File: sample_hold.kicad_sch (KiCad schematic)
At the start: 44 parts, among them K21 G6K-2FY, 5V, Q201 AO3400A, Q202 AO3401A, Q203 AO3400A, Q204 AO3400A, Q205 AO3400A, Q206 AO3400A, Q207 AO3400A, U19 TCA0372, U21 OPA828DGN, U22 OPA2197D, U23 DG419D

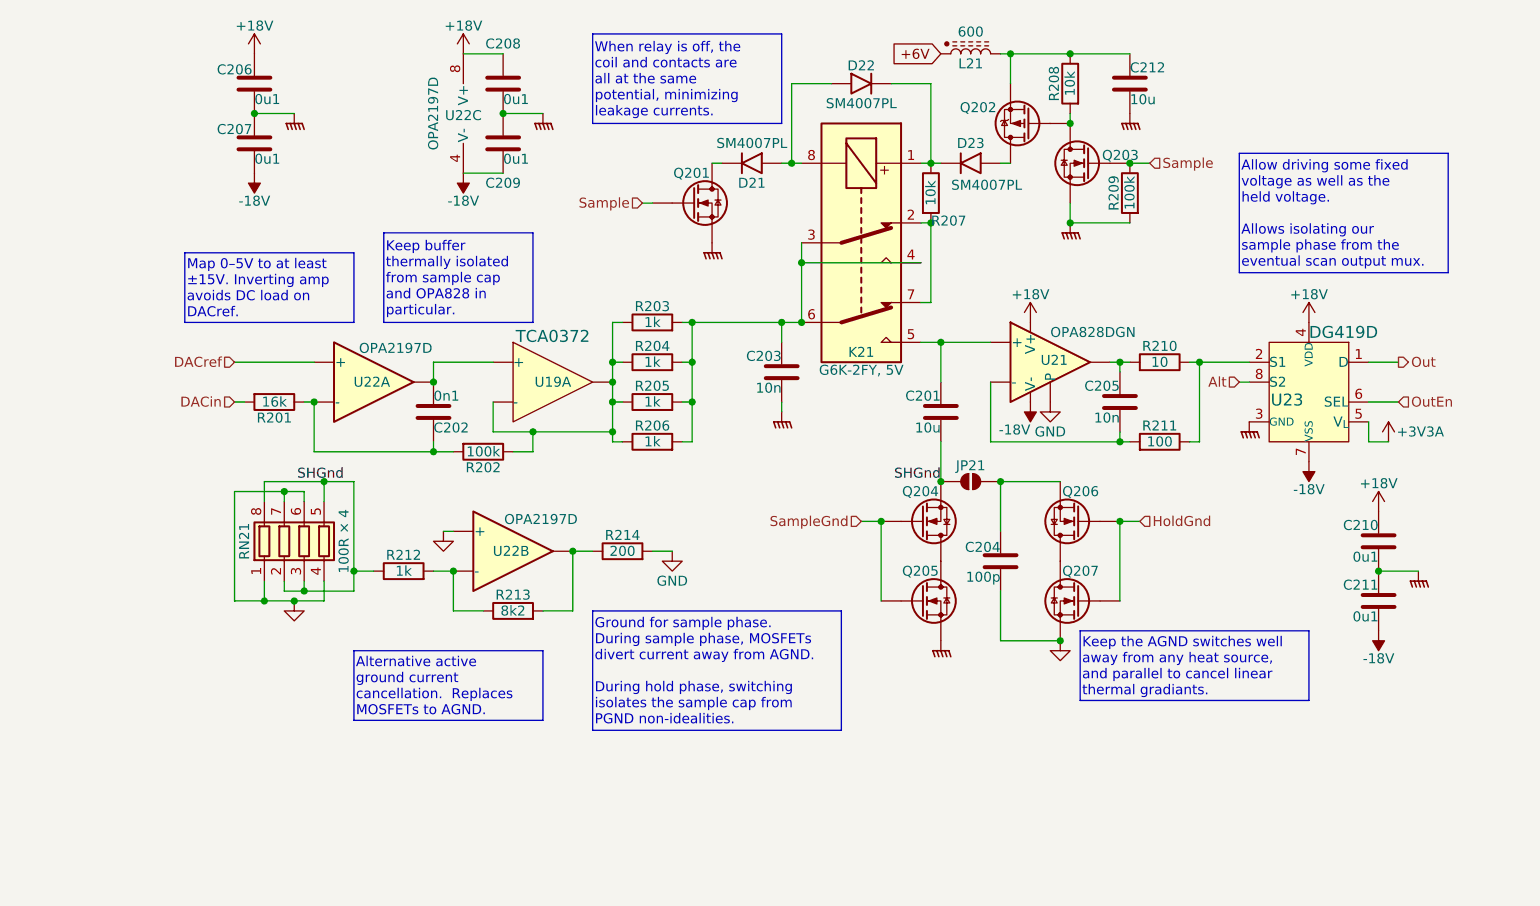
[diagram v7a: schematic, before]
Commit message: Whew.  DACs routed
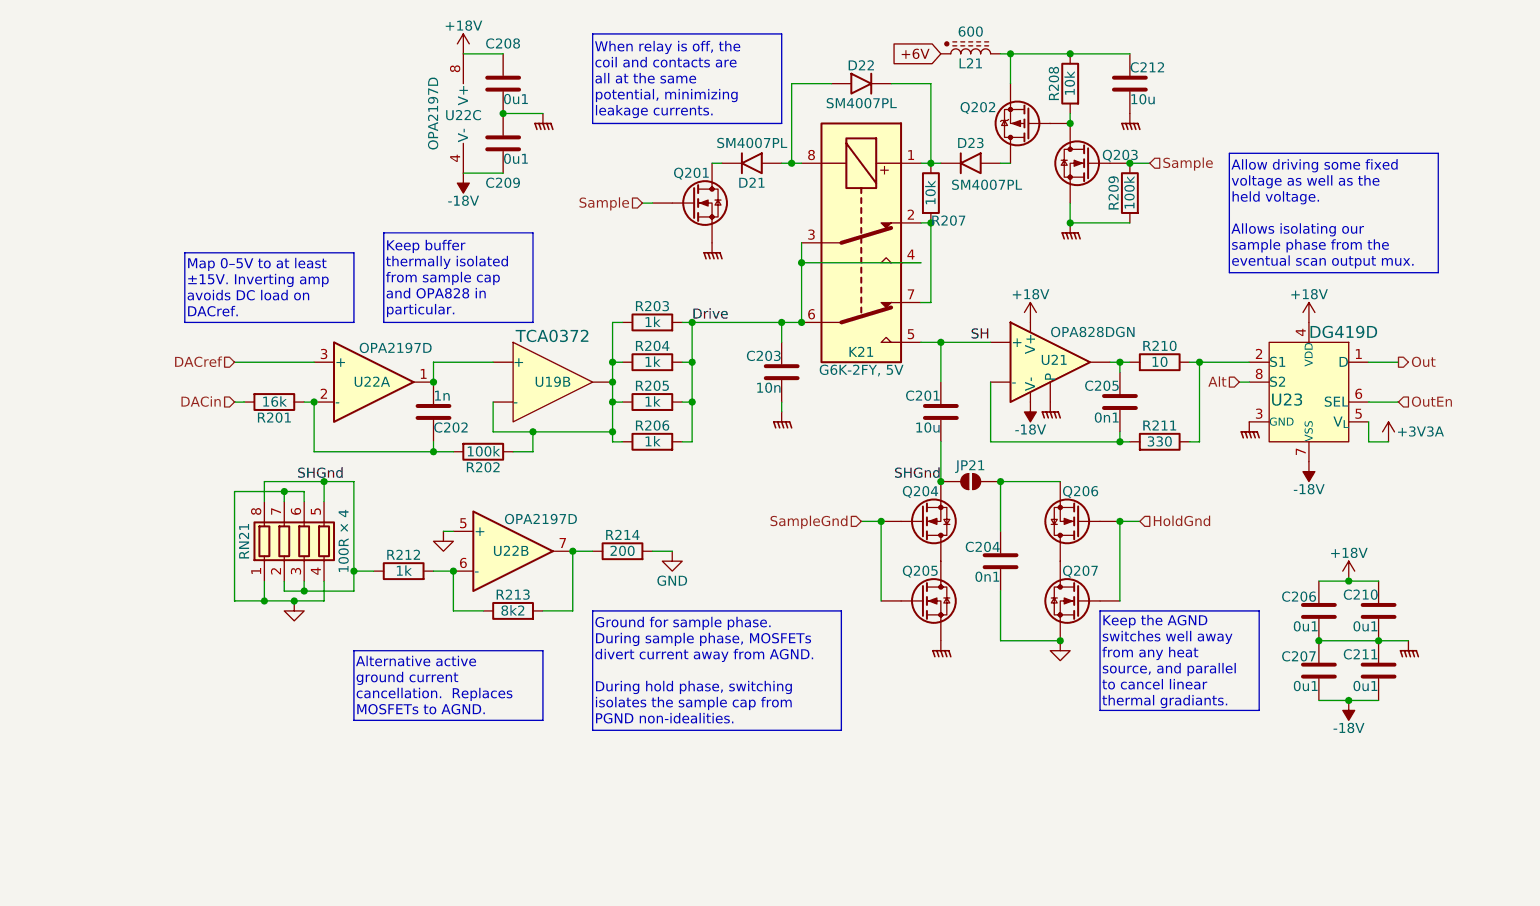
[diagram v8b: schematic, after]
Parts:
- C201: footprint Capacitor_THT:C_Rect_L31.5mm_W15.0mm_P27.50mm_MKS4 -> Parts:C_Rect_L31.5mm_W15.0mm_P27.50mm_MKS4
- C202: value 0n1 -> 1n; footprint Capacitor_SMD:C_0603_1608Metric -> Capacitor_SMD:C_0402_1005Metric; LCSC C14858 -> C1523
- C204: value 100p -> 0n1
- C205: value 10n -> 0n1; footprint Capacitor_SMD:C_0603_1608Metric -> Capacitor_SMD:C_0402_1005Metric; LCSC C307500 -> C1546
- Q201, Q202, Q203, Q204, Q205, Q206, Q207: footprint Package_TO_SOT_SMD:SOT-23 -> Parts:SOT-23
- R211: value 100 -> 330; LCSC C25076 -> C25104
- U21: footprint Package_SO:HVSSOP-8-1EP_3x3mm_P0.65mm_EP1.57x1.89mm -> Parts:VSSOP-8-1EP_3x3mm_P0.65mm_EP1.57x1.89mm
- U22: footprint Package_SO:SOIC-8_3.9x4.9mm_P1.27mm -> Parts:OPA2197; symbol Amplifier_Operational:OPA2197xD -> Parts:OPA2197D
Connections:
- net GND: no longer U21.9 (P)
- net GNDPWR: now also U21.9 (P)
- net at R202.1, R203.1, R204.1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: now also U19.2, U19.7 (-); no longer U19.10 (-), U19.16
- net at C202.2, U22.1: now also U19.8 (+); no longer U19.9 (+)
- net Drive: now reaches C203.2, K21.3, K21.4, K21.6, R203.2, R204.2, R205.2, R206.2
- net SH: now reaches C201.1, K21.5, U21.3 (+)
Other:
- moved on the sheet: C206, C207, C210, C211
